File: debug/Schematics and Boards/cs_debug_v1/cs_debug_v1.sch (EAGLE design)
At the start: 241 parts, among them J1 J-JTAG-CORTEX_SMD, J19 Solar, J2 J-JTAG-CORTEX_SMD, J3 J-JTAG-CORTEX-NEEDLE6-LEGS, J4 J-SERIAL-PORT, J5 J-WURTH-USBC, Q10 2N7002P, Q3 FDN340P, Q4 2N7002P, Q5 FDN340P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

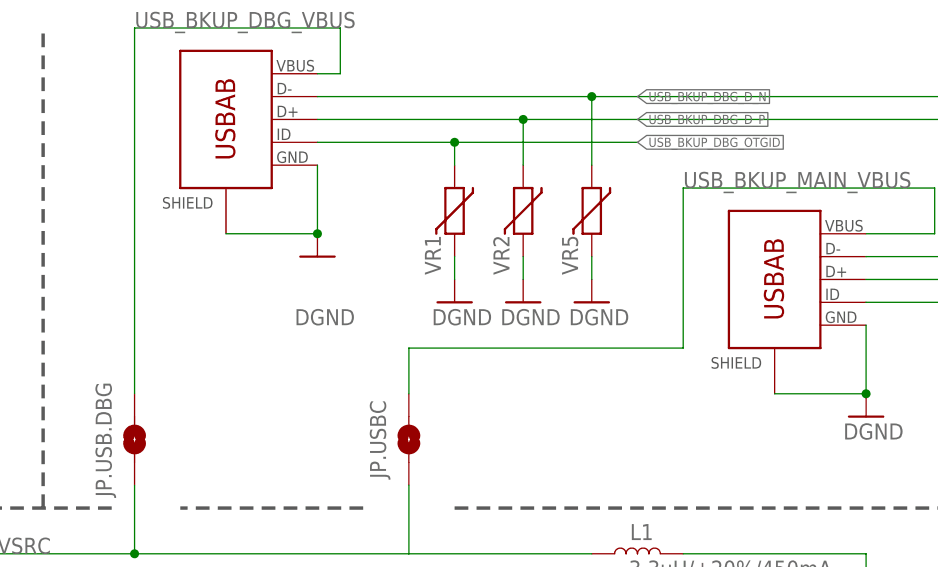
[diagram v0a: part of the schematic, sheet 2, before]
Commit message: DBG: Fix DFM issues for 7PCB
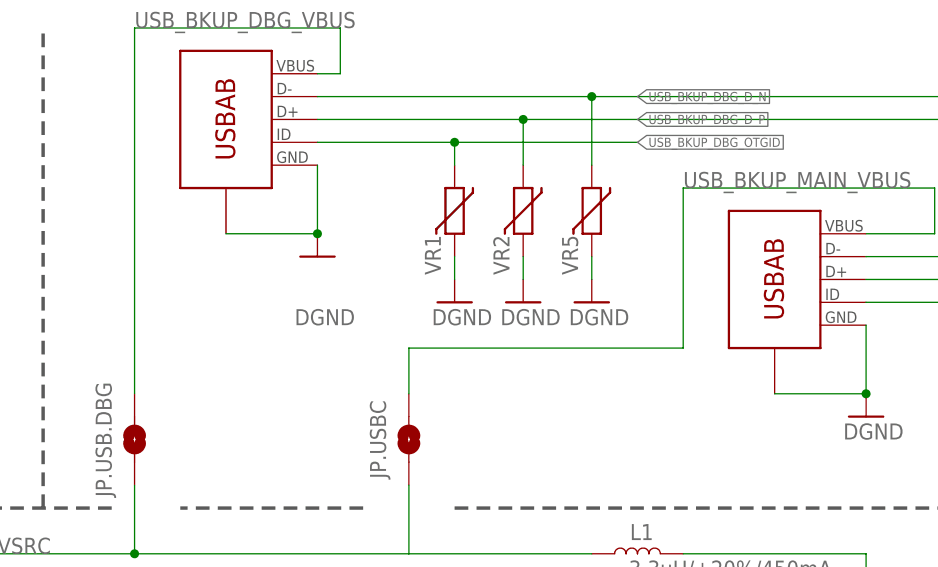
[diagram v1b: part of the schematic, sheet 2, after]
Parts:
- J.USB.DBG, J.USB.MN: value USBABSMTDIP -> J-USB-HIROSE-MICRO-USB; device ZX62D-AB-5P8:USBABSMTDIP -> Connectors:J-USB-HIROSE-MICRO-USB
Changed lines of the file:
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@@
 <part name="SDA" library="TestPoints" deviceset="TP" device="TP10SQ" package3d_urn="urn:adsk.eagle:package:27962/1"/>
 <part name="D2" library="Diodes" deviceset="BGX50A" device=""/>
-<part name="J.USB.DBG" library="ZX62D-AB-5P8" deviceset="USBABSMTDIP" device="">
+<part name="J.USB.DBG" library="Connectors" deviceset="J-USB-HIROSE-MICRO-USB" device="">
 <attribute name="MP" value="ZX62D-AB-5P8(30)"/>
 <attribute name="MPN" value="ZX62D-AB-5P8(30)"/>
@@
 <part name="GND207" library="Supplies" deviceset="GND" device=""/>
 <part name="GND210" library="Supplies" deviceset="GND" device=""/>
-<part name="J.USB.MN" library="ZX62D-AB-5P8" deviceset="USBABSMTDIP" device="">
+<part name="J.USB.MN" library="Connectors" deviceset="J-USB-HIROSE-MICRO-USB" device="">
 <attribute name="MP" value="ZX62D-AB-5P8(30)"/>
 <attribute name="MPN" value="ZX62D-AB-5P8(30)"/>
